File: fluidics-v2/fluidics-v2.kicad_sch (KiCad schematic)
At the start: 35 parts, among them J1 PJ-063AH, J10 87832-1010, J11 0705430001, J12 87832-1010, J13 0705430001, J14 87832-1010, J15 0533980671, J16 0705430001, J17 0533980671, J18 87832-1010, J19 0705430001, J2 0533980671, J20 0533980671, J21 87832-1010, J22 0705430001, J23 0533980671, J3 A-DS_15_A_KG-T4S, J4 0533980671, J5 1860280, J6 Conn_02x14_Counter_Clockwise, J7 Conn_02x03_Odd_Even, J8 5031543090, U2 Teensy4.1

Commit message: finished schematic
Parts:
- removed J8: 5031543090, 5031543090:CON_5031543090, symbol 5031543090:5031543090
- added J8: 705430039, 70543-0039_MOL, symbol 0705430004:705430039
- added J9: 522712079, 0522712079:CON_522712079_MOL, symbol 0522712079:522712079
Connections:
- net I2C_SCL is gone; now on net SDA: TP1.1
- net I2C_SDA is gone; now on net SCL: TP1.2
- net Power Supplies/PG-12V is gone; now on net GPIO_8: U2.7 (5_IN2)
- net Power Supplies/PG-5V is gone; now on net ~{INVALID}_SYRPUMP: U2.8 (6_OUT1D)
- net +12V: now also J8.3
- net +24V: now also J8.2
- net +3.3V: now also J8.5
- net +5V: now also J8.4
- net GND: now also J8.1, J9.20, J9.P1, J9.P2
- net GPIO_0: now also J9.10
- net GPIO_1: now also J9.9
- net GPIO_2: now also J9.8
- net GPIO_3: now also J9.7
- net GPIO_4: now also J9.6
- net GPIO_5: now also J9.5
- net GPIO_6: now also J9.4
- net GPIO_7: now also U2.30 (38_CS1_IN1), J9.3; no longer U2.25 (33_MCLK2)
- net GPIO_8: now also J9.2; no longer U2.24 (32_OUT1B)
- net GPIO_9: now also J9.1
- net SCL: now also J9.18
- net SCL1: now also J9.16
- net SCL2: now also J9.14
- net SDA: now also J9.19
- net SDA1: now also J9.17
- net SDA2: now also J9.15
- net SPI_MISO: now also J9.12
- net SPI_MOSI: now also J9.13
- net SPI_SCK: now also J9.11
- net UART_RX_DISCPUMP: now also U2.36 (14_A0_TX3_SPDIF_OUT); no longer U2.10 (8_TX2_IN1)
- net UART_RX_SYRPUMP: now also U2.10 (8_TX2_IN1); no longer U2.36 (14_A0_TX3_SPDIF_OUT)
- net UART_TX_DISCPUMP: now also U2.37 (15_A1_RX3_SPDIF_IN); no longer U2.9 (7_RX2_OUT1A)
- net UART_TX_SYRPUMP: now also U2.9 (7_RX2_OUT1A); no longer U2.37 (15_A1_RX3_SPDIF_IN)
- net ~{INVALID}_SYRPUMP: no longer U2.30 (38_CS1_IN1)
- new net PG-12V: U2.24 (32_OUT1B)
- new net PG-5V: U2.25 (33_MCLK2)
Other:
- note added: "Connections for powering the daughter board"

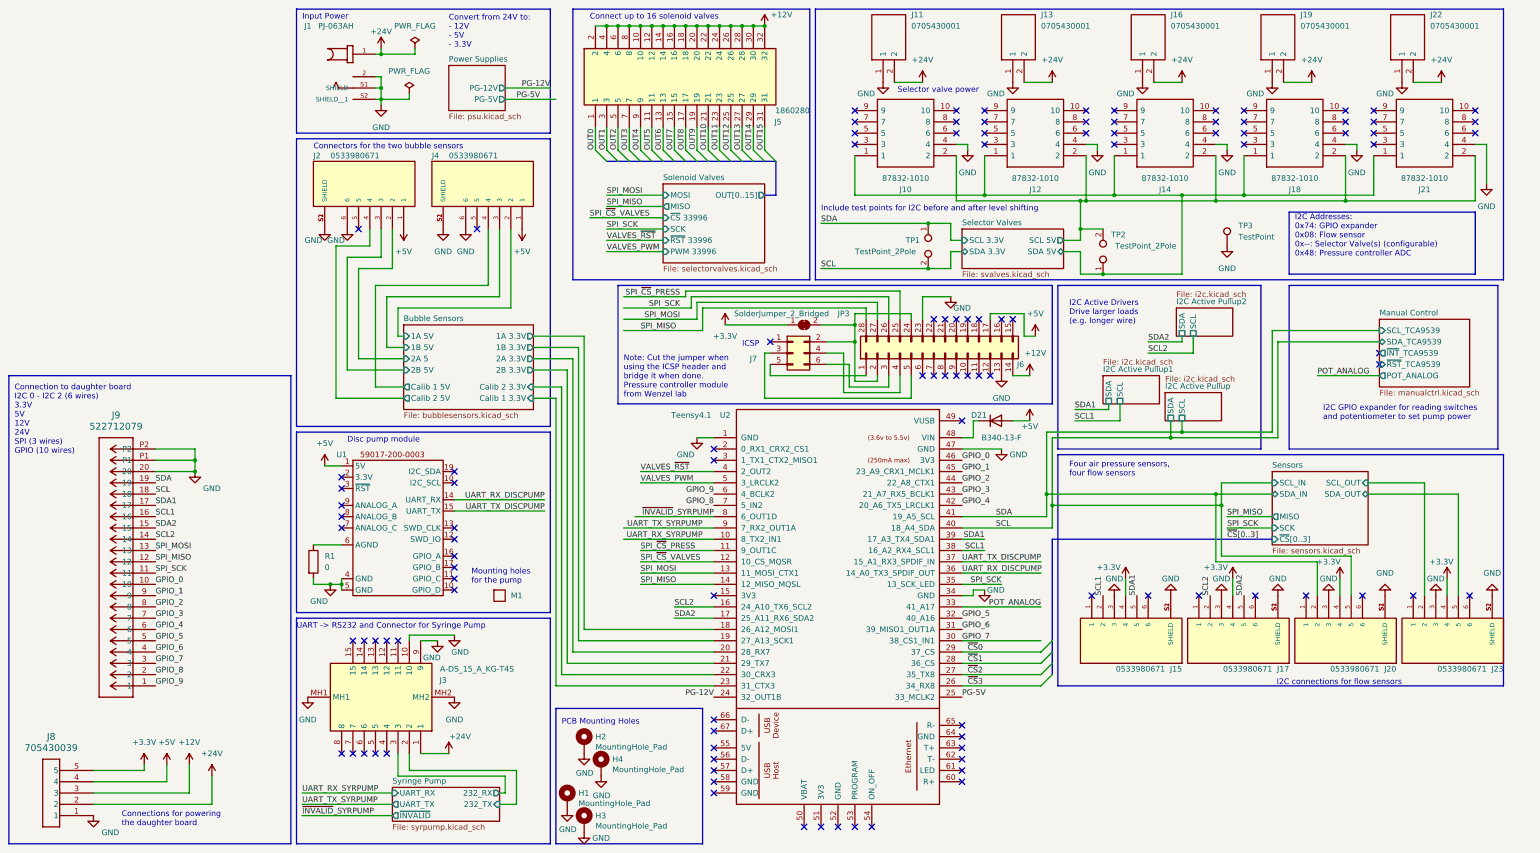
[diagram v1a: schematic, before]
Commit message: added pullups/downs to spi for stability, rounded corners
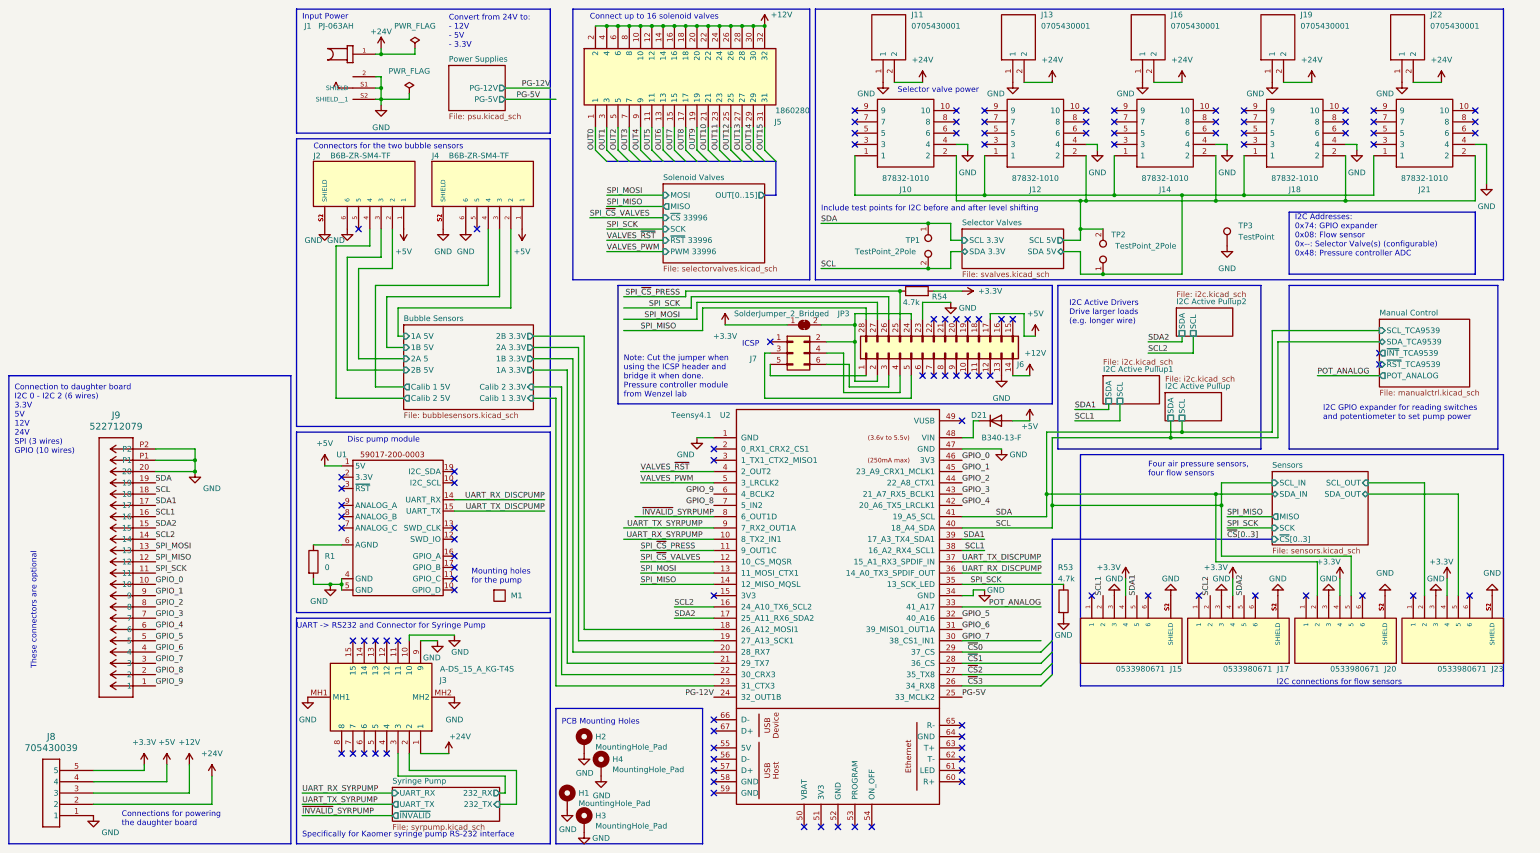
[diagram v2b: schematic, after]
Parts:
- added R53, R54: 4.7k, Resistor_SMD:R_0402_1005Metric, symbol Device:R
- J1: LCSC (none) -> C2928097
- J11, J13: LCSC (none) -> C5349069
- J2, J4: value 0533980671 -> B6B-ZR-SM4-TF; footprint molex_connectors:MOLEX_0533980671 -> B6B-ZR-SM4-TF:CONN_B6B-ZR-SM4-TF_JST; MANUFACTURER Molex -> JST; MAXIMUM_PACKAGE_HEIGHT 4.7mm -> (none); PARTREV A -> (none); STANDARD Manufacturer Recommendations -> (none)
- J3: LCSC (none) -> C3100941
- J8: LCSC (none) -> C588438
- J9: LCSC (none) -> C588186
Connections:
- net +3.3V: now also R54.2
- net Bubble Sensors/1A 3.3V: now also U2.21 (29_TX7); no longer U2.18 (26_A12_MOSI1)
- net Bubble Sensors/1B 3.3V: now also U2.20 (28_RX7); no longer U2.19 (27_A13_SCK1)
- net Bubble Sensors/2A 3.3V: now also U2.19 (27_A13_SCK1); no longer U2.20 (28_RX7)
- net Bubble Sensors/2B 3.3V: now also U2.18 (26_A12_MOSI1); no longer U2.21 (29_TX7)
- net GND: now also R53.2
- net SPI_SCK: now also R53.1
- net SPI_~{CS}_PRESS: now also R54.1
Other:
- note added: "Specifically for Kaomer syringe pump RS-232 interface"
- note added: "These connectors are optional"

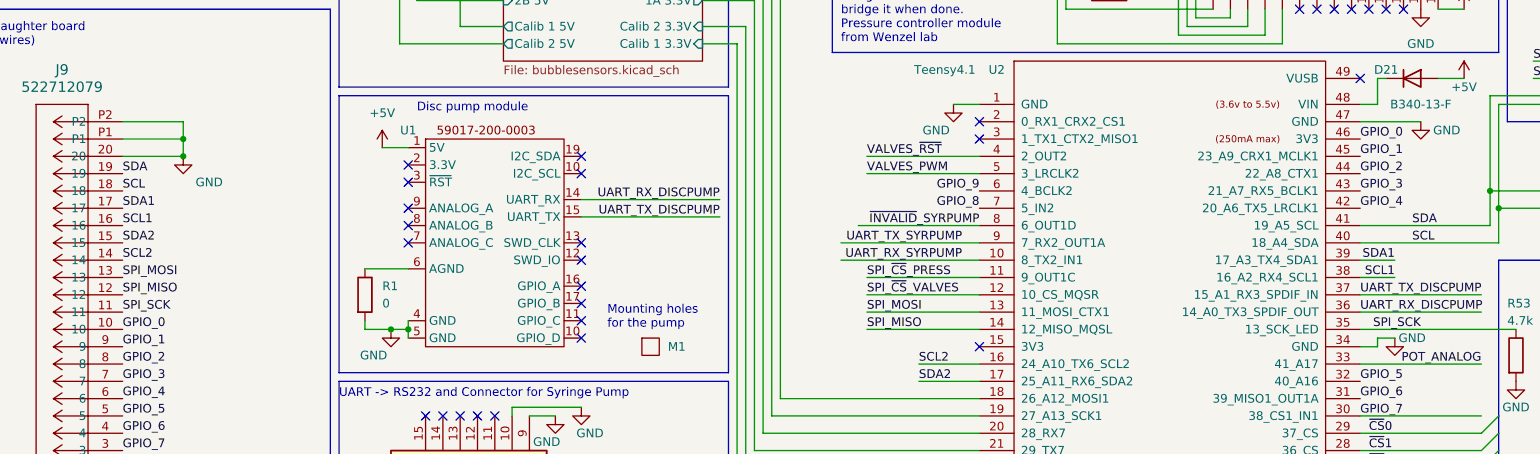
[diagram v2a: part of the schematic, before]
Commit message: fixed error on 3.3V line, added extra ground to fpc
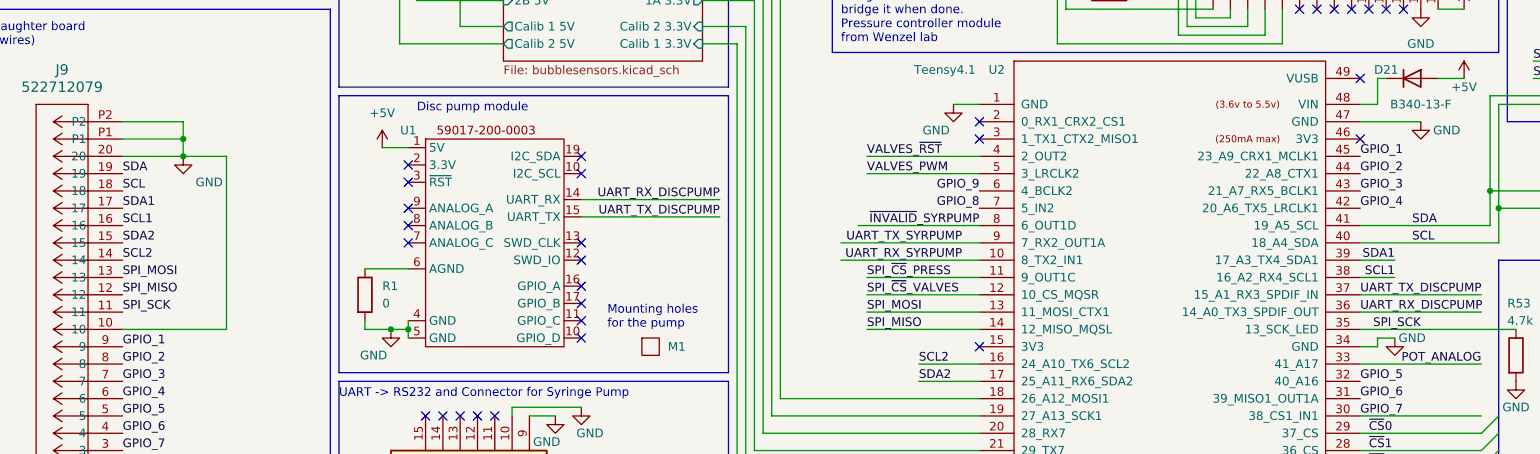
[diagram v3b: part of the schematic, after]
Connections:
- net GND: now also J9.10
- net GPIO_0: no longer names the net of U2.46 (3V3)
- net GPIO_0: no longer J9.10
- no-connect marks 107 -> 108
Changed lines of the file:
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@@
   (no_connect (at 341.63 121.92))
   (no_connect (at 170.18 222.25))
+  (no_connect (at 284.48 198.12))
   (no_connect (at 260.35 121.92))
   (no_connect (at 228.6 273.05))
@@
     (stroke (width 0) (type default))
   )
+  (wire (pts (xy 118.11 200.66) (xy 111.76 200.66))
+    (stroke (width 0) (type default))
+  )
   (wire (pts (xy 209.55 123.19) (xy 209.55 128.27))
     (stroke (width 0) (type default))
@@
     (stroke (width 0) (type default))
   )
+  (wire (pts (xy 118.11 226.06) (xy 118.11 200.66))
+    (stroke (width 0) (type default))
+  )
   (wire (pts (xy 237.49 123.19) (xy 237.49 128.27))
     (stroke (width 0) (type default))
@@
   )
   (wire (pts (xy 187.96 175.26) (xy 196.85 175.26))
+    (stroke (width 0) (type default))
+  )
+  (wire (pts (xy 102.87 226.06) (xy 118.11 226.06))
     (stroke (width 0) (type default))
   )
@@
     (effects (font (size 1.27 1.27)) (justify left bottom))
   )
-  (label "GPIO_0" (at 102.87 226.06 0) (fields_autoplaced)
-    (effects (font (size 1.27 1.27)) (justify left bottom))
-  )
   (label "SCL2" (at 340.36 228.6 90) (fields_autoplaced)
     (effects (font (size 1.27 1.27)) (justify left bottom))
@@
     (effects (font (size 1.27 1.27)) (justify left bottom))
   )
-  (label "GPIO_0" (at 284.48 198.12 0) (fields_autoplaced)
-    (effects (font (size 1.27 1.27)) (justify left bottom))
-  )
